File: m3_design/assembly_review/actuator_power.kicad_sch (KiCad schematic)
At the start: 15 parts, among them Q120 AON6403, Q121 AON6403, Q122 AO3400A

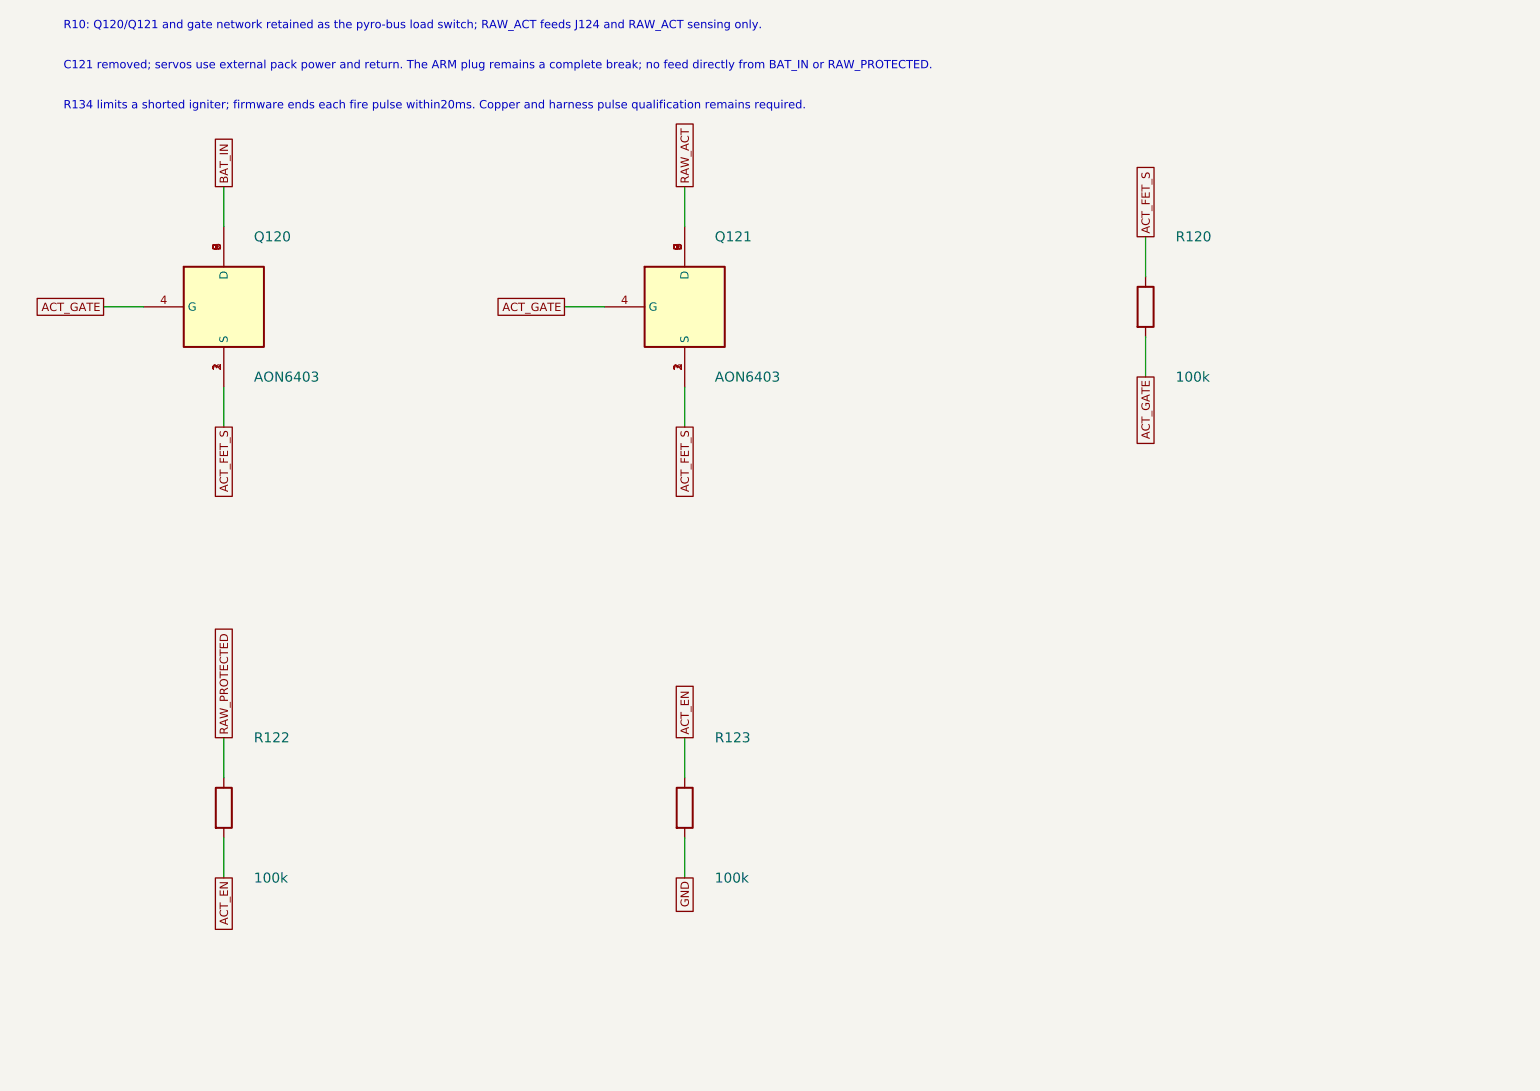
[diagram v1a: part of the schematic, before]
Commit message: R10 single screw-switch arming pass before review round 9
Preparatory single-switch pass, not a full review round or clean-round credit.
Remove J124 and its fused ARM link, join the post-switch bus as RAW_ACT, and
implement the independent PC1 load-switch enable through R122/Q122 while PE4
controls the fire FET. Move R134 for direct bottom-side fire routing. Update
schematic/PCB generators, contracts, seeded tests, binding and operating records.
No interrupted changes were discarded. AUD/GAP cuts and fresh round 9 follow.

Board SHA-256: 60be35eaff86dd7a5fb8e065aa4204a51e7d786d7dfc8d2456cdd66c4b86f901
Board: 46 x 90 mm, 4 layers, 2521622 bytes. Two full builds are byte-identical.
Netlist SHA-256: 3e08722d7ac997131cb11d7c9cb2d25e1b3babcfb853b71230db01118bc70e69
Fab: 228 CPL rows, 83 BOM lines; orientation, paste and manifest checks pass.
Hot-plug: same input-feed signature; 2304 corners and local sensitivities pass
(simulation / Inference). Bench, firmware, RF immunity and physical fit unverified.

Final unskipped tools/check.sh: exit 0
DRC violations 0  unconnected 0  schematic parity 0  ERC 0
metadata / 3D model audit: OK
fit check: OK (CAD envelopes only)
R10 CAD contract (full): OK
routing hygiene: 0 failing, 0 allowlisted, 0 leftovers recorded
actuator safety contract: OK
Fab manifest: OK; 5 outputs match the current CAD and export inputs
Self-tests: shell 4, fit 23, paste 5, route 57; R10 122 (3 NumPy tests
skipped in KiCad Python then passed separately). Standalone plate 3 passed.
Added local absolute paths: 0. No direct Git index/commit mutation performed.

Co-Authored-By: Claude Opus 5.5 <noreply@anthropic.com>
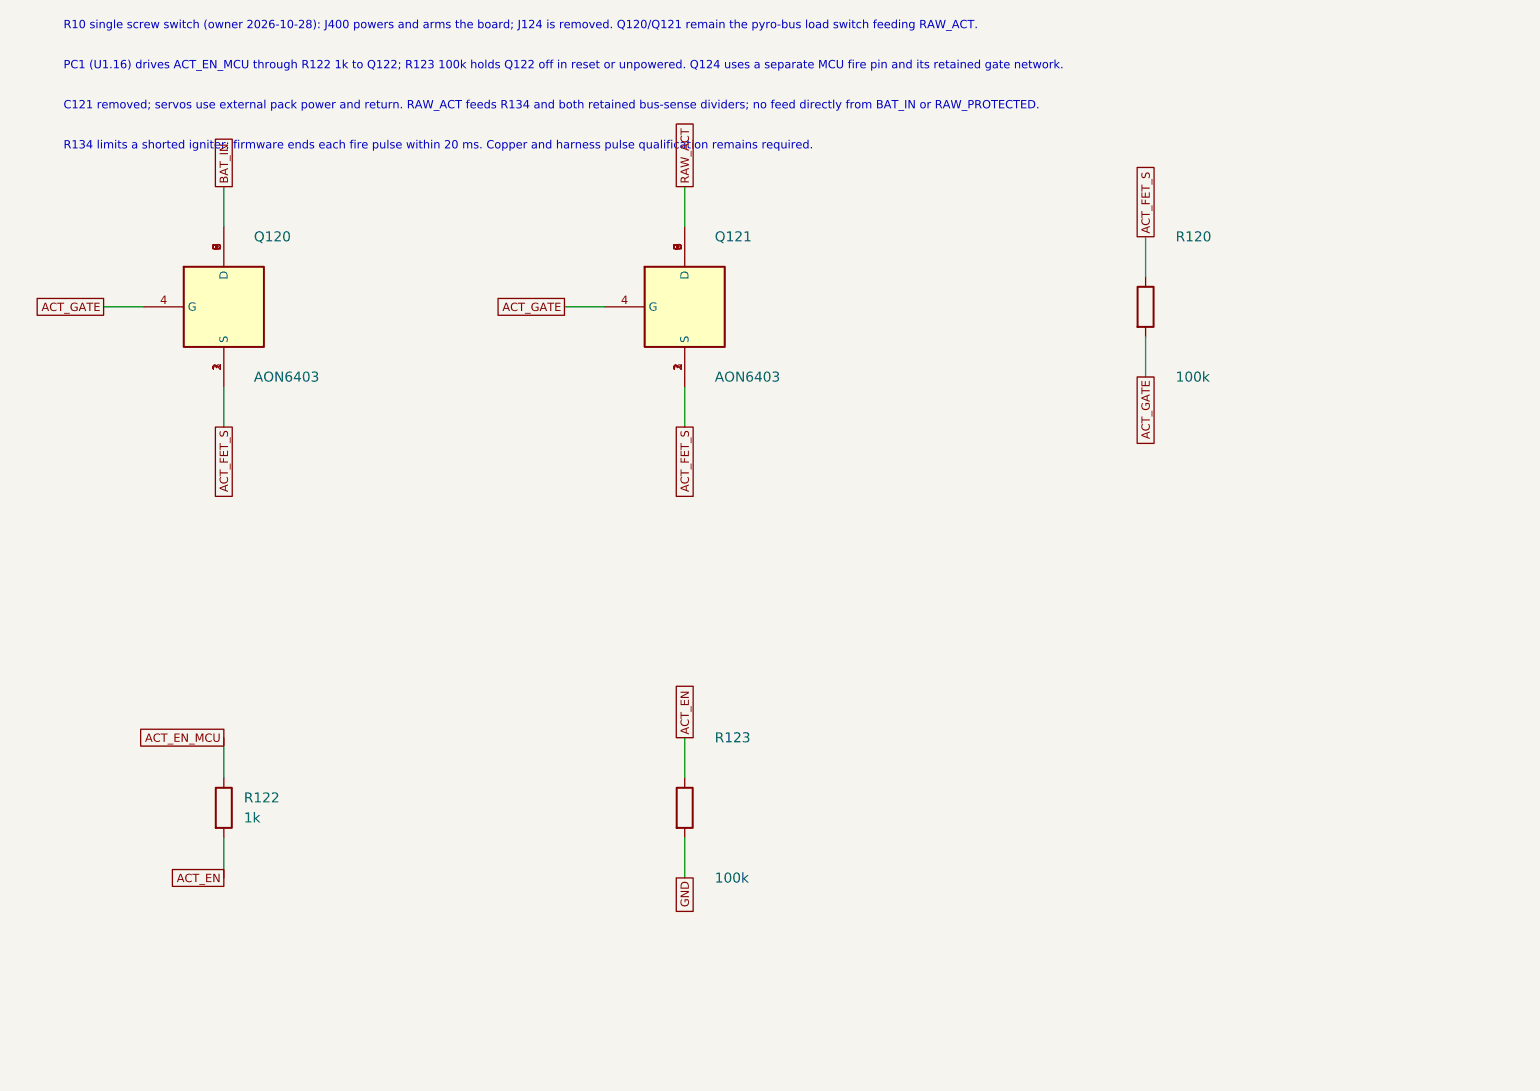
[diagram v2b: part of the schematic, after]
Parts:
- R122: value 100k -> 1k; LCSC C25741 -> C11702; Manufacturer Part 0402WGF1003TCE -> 0402WGF1001TCE
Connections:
- net RAW_PROTECTED renamed ACT_EN_MCU
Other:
- note added: "C121 removed; servos use external pack power and return. RAW_ACT feeds R134 and both retained bus-sense dividers; no feed directly from BAT_IN or RAW_PROTECTED."
- note added: "PC1 (U1.16) drives ACT_EN_MCU through R122 1k to Q122; R123 100k holds Q122 off in reset or unpowered. Q124 uses a separate MCU fire pin and its retained gate network."
- note added: "R10 single screw switch (owner 2026-10-28): J400 powers and arms the board; J124 is removed. Q120/Q121 remain the pyro-bus load switch feeding RAW_ACT."
- note added: "R134 limits a shorted igniter; firmware ends each fire pulse within 20 ms. Copper and harness pulse qualification remains required."
- note removed: "C121 removed; servos use external pack power and return. The ARM plug remains a complete break; no feed directly from BAT_IN or RAW_PROTECTED."
- note removed: "R10: Q120/Q121 and gate network retained as the pyro-bus load switch; RAW_ACT feeds J124 and RAW_ACT sensing only."
- note removed: "R134 limits a shorted igniter; firmware ends each fire pulse within20ms. Copper and harness pulse qualification remains required."

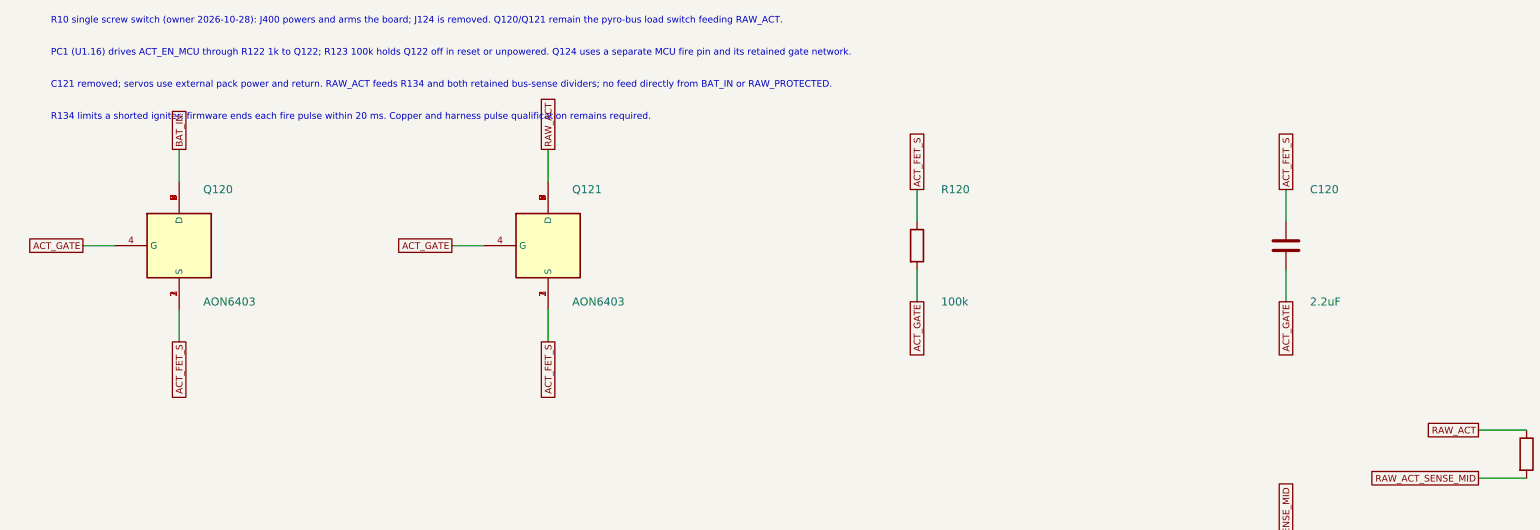
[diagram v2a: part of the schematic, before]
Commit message: R10 requirements-audit cuts and GAP fixes before review round 9
Implement adopted AUD-1 through AUD-10 and GAP-1 through GAP-5 after the single-switch pass.
Remove the advisory pull-pin, redundant probes and GPS/radio IO LDO cells; qualify the smaller
AONR21357 pair, correct C120 voltage rating, standardize shared-code capacitor lands, simplify
slow returns and fire-only copper, localize U9 output protection and add exactly two U401 VIPPO vias.
Record physical-current timing, coupled fire/source budget, C84 manual fitting and narrowed gate scopes.

Board SHA-256: 877d01996a59e9dd5c6dbc367274bb9a323a13982d67960fe46df9b0ee53205d
Board: 46 x 90 mm, 4 layers, 2365477 bytes; 225 footprints, 883 straight tracks, 323 vias.
Netlist SHA-256: 0843da709e2d7a757e9b35cdff48158a54012c5353619cbf409ab961efd2c3ca
Two fresh complete passing builds are byte-identical. Schematic: 700 pins; 22 seeded faults detected.

Final unskipped tools/check.sh: exit 0
DRC violations 0  unconnected 0  schematic parity 0  ERC 0
metadata / 3D model audit: OK
silkscreen outside the board outline: 0 stroke points
fit check: OK (CAD envelopes only)
R10 CAD contract (full): OK
routing hygiene: 0 failing, 0 allowlisted, 0 leftovers recorded
actuator safety contract: OK
Fab manifest: OK; 5 outputs match current CAD and export inputs
Self-tests: shell 4, fit 24, paste 5, routing 59, R10 131; three NumPy cases rerun and passed.

Fab: 215 CPL rows, 82 BOM codes; orientation / paste / manifest pass. Hot-plug: 2304 required
cases plus convergence and controls pass (simulation / Inference). Plate f1 280.9 Hz (Inference).
Live JLC: $84.43 vs $84.41 target, 46 Extended codes; R430 / U4 short. Procurement exit 1 is a
disclosed OQ-3 / ordering deviation, not a CAD gate pass. No quote accepted or order placed.
Firmware, bench, thermal/transient correlation, process acceptance, installed RF immunity and physical fit unverified.

This preparatory pass earns no clean-review credit. Start fresh full ten-lens round 9 on th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
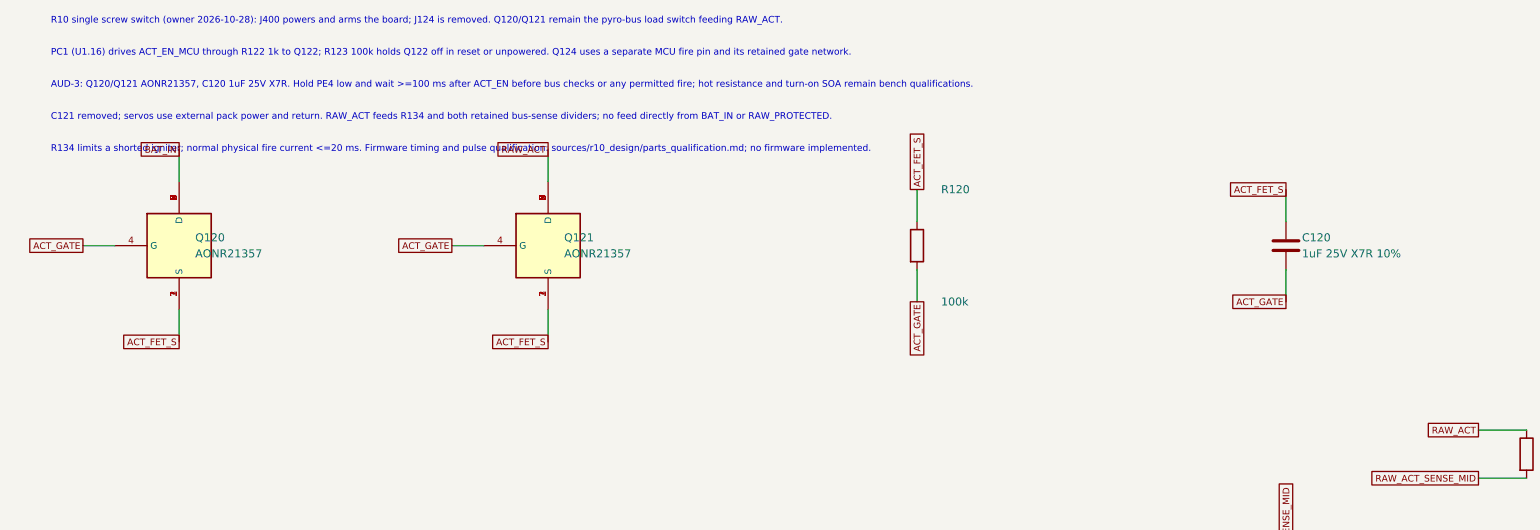
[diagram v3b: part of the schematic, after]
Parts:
- C120: value 2.2uF -> 1uF 25V X7R 10%; footprint rocket:C0603 -> rocket:C_0603_1608Metric; LCSC C23630 -> C29936; Manufacturer Part CL10A225KO8NNNC -> CL10B105KA8NNNC
- Q120, Q121: value AON6403 -> AONR21357; footprint rocket:PDFN-8_L5.6-W5.2-P1.27-LS6.1-BL -> rocket:M3_AONR21357_DFN3x3A_EP1; LCSC C2760089 -> C431196; Manufacturer Part AON6403 -> AONR21357
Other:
- note added: "AUD-3: Q120/Q121 AONR21357, C120 1uF 25V X7R. Hold PE4 low and wait >=100 ms after ACT_EN before bus checks or any permitted fire; hot resistance and turn-on SOA remain bench qualifications."
- note added: "R134 limits a shorted igniter; normal physical fire current <=20 ms. Firmware timing and pulse qualification: sources/r10_design/parts_qualification.md; no firmware implemented."
- note removed: "R134 limits a shorted igniter; firmware ends each fire pulse within 20 ms. Copper and harness pulse qualification remains required."
